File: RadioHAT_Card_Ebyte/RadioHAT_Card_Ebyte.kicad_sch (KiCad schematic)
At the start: 9 parts

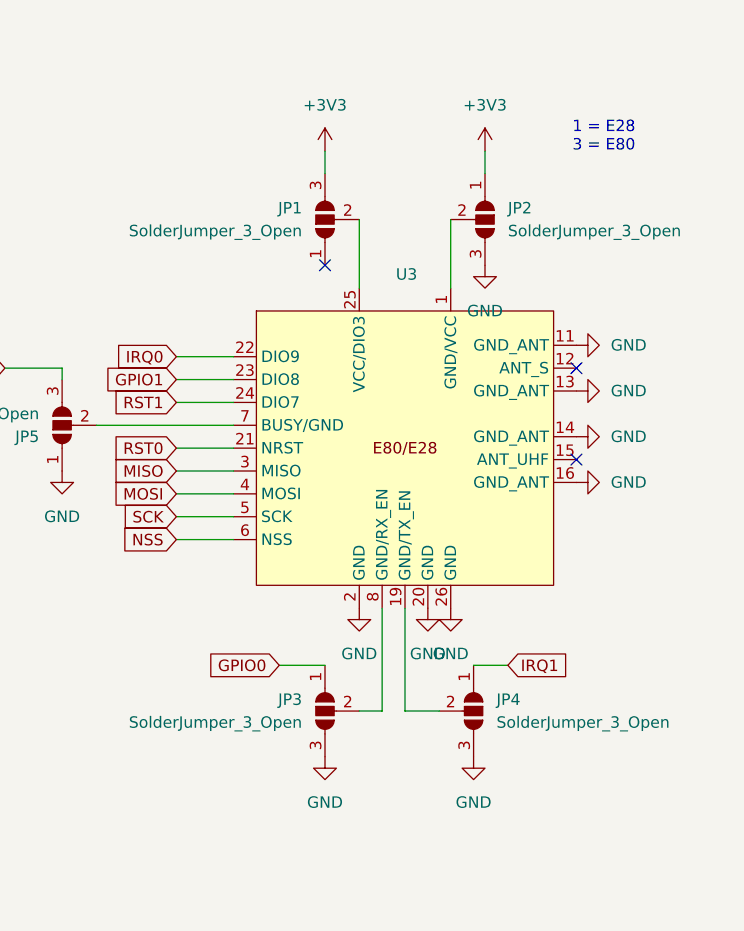
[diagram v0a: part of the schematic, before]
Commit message: [SCH] Fix power flags
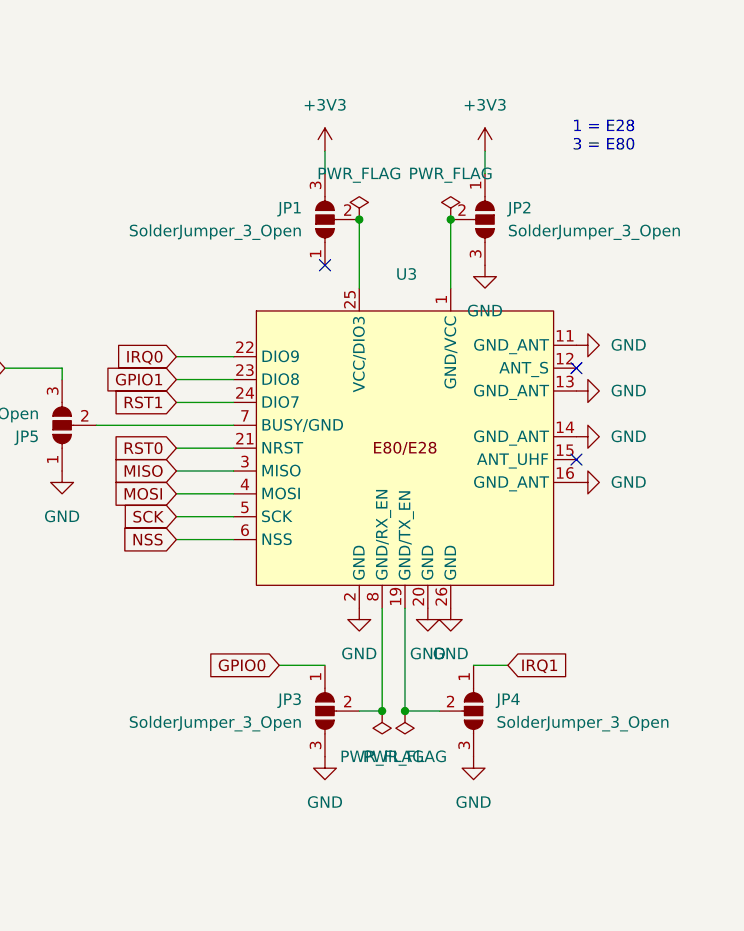
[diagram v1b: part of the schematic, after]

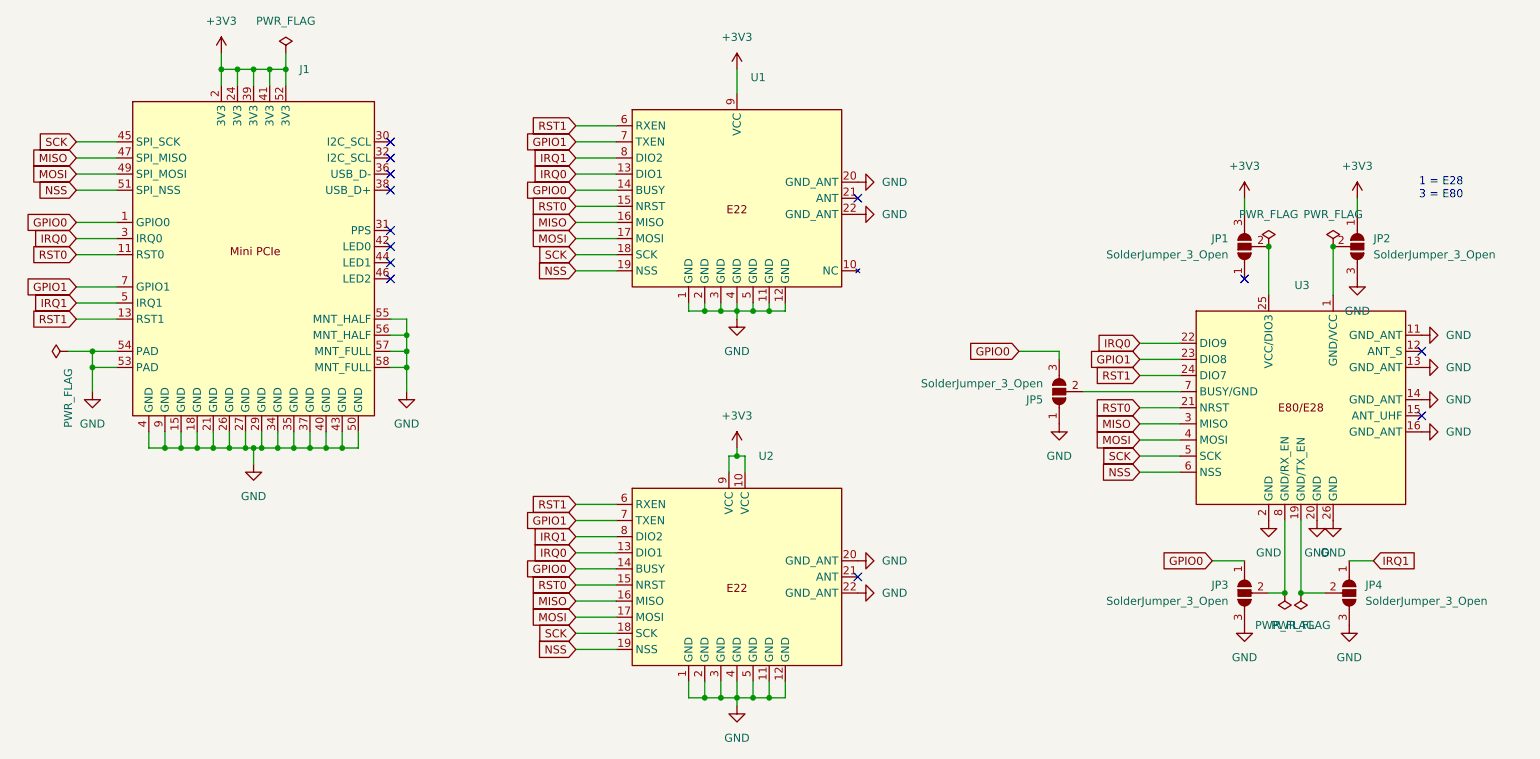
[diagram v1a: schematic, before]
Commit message: Update symbols to align with library
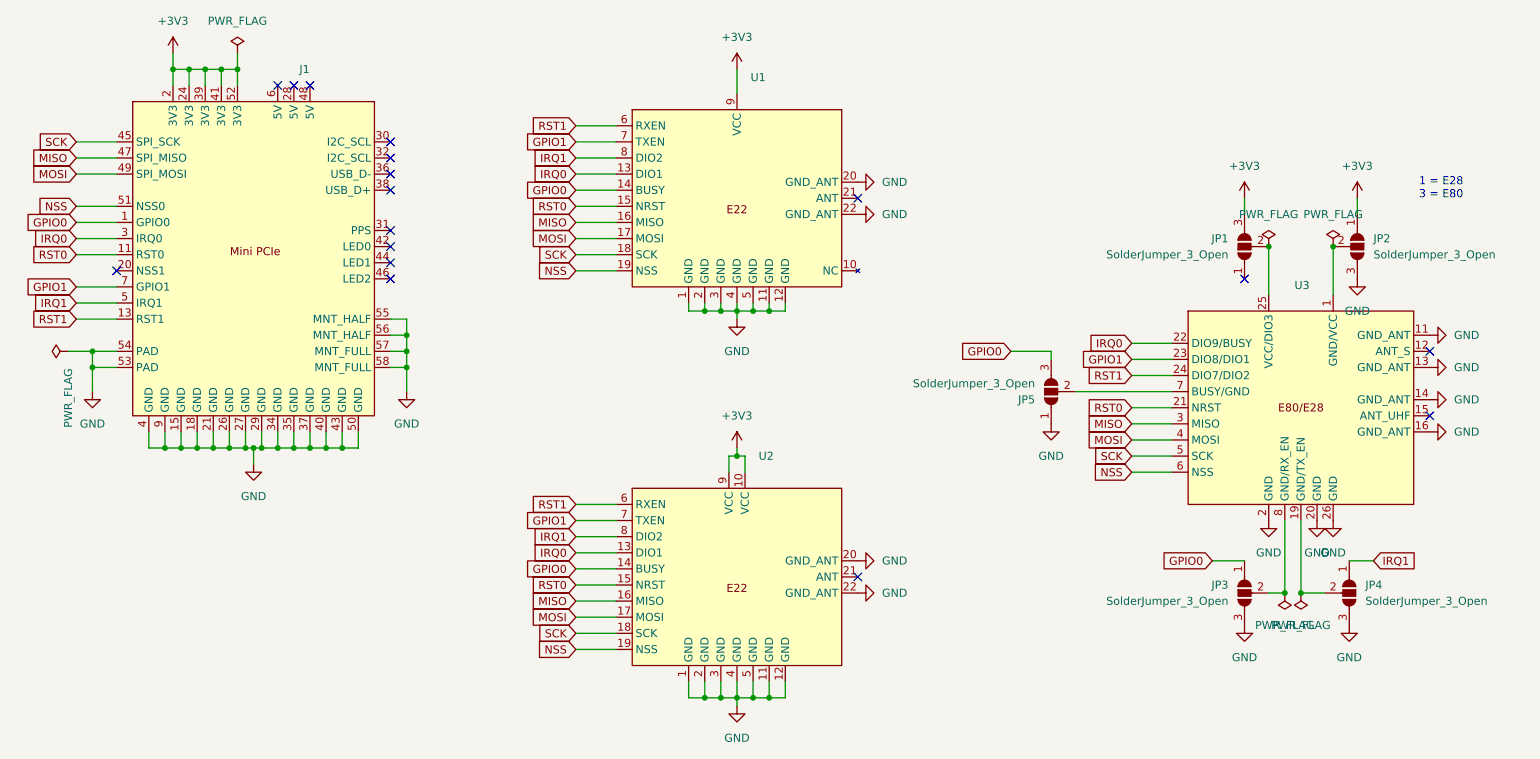
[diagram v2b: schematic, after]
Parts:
- J1: Mouser (none) -> 571-1775838-2
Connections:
- no-connect marks 13 -> 17
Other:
- moved on the sheet: JP5
